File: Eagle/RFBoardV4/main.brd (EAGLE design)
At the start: 34.3 x 77.5 mm, 28 parts, among them Q1 8/16/20MHz, U1 ATMEGA328

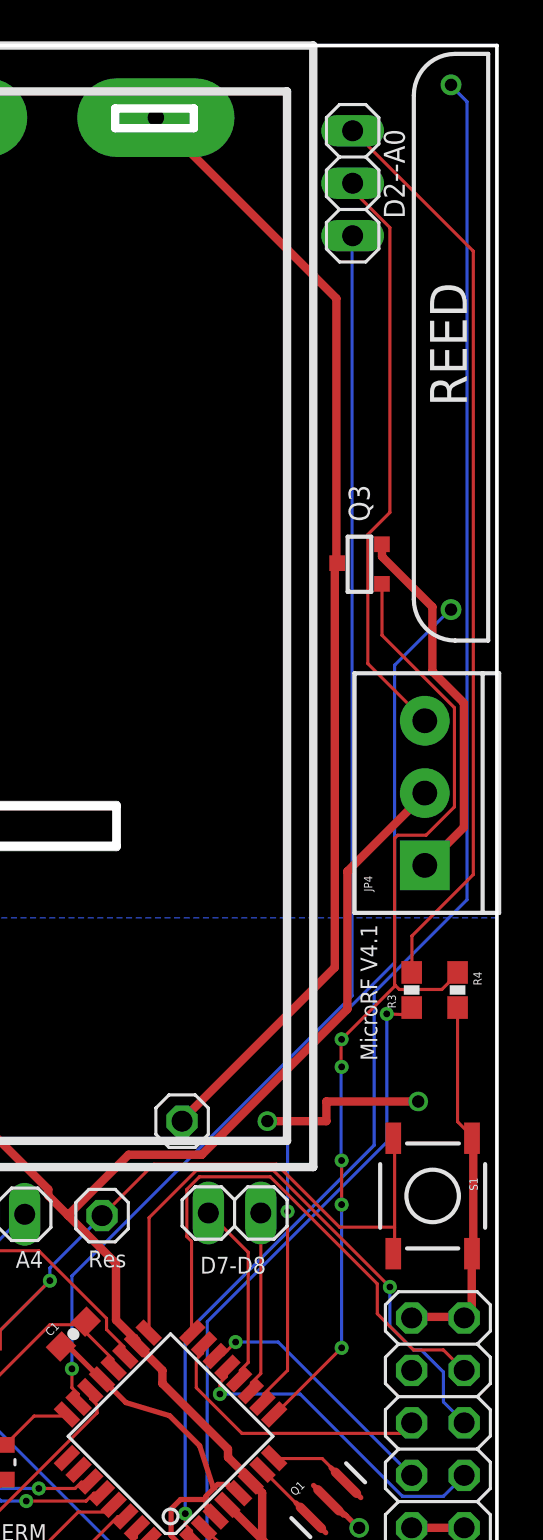
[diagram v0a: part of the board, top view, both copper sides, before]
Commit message: 4.x support + 4.1 pcb layout + cleanup
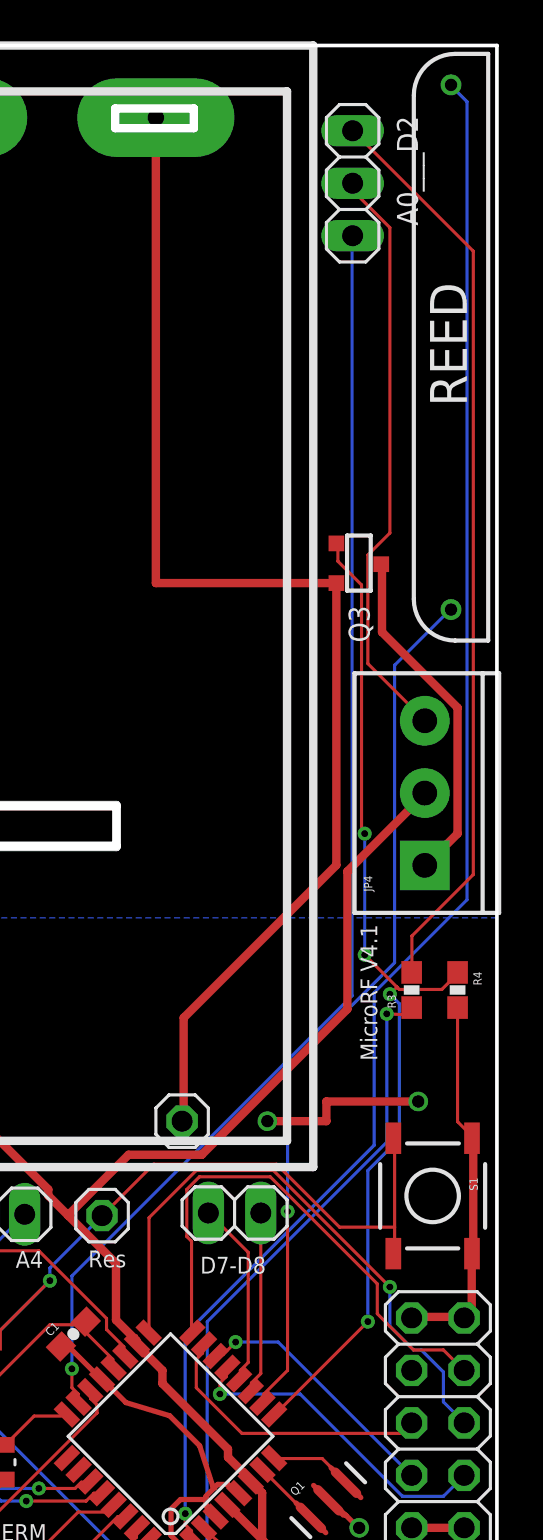
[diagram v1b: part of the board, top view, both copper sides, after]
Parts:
- turned Q3 to 270 degrees
- renumbered BATMIN to GND, BATPLUS to VCC(3V), D2--A0 to A0___D2
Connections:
- removed net SCREW_GND: JP4.1, Q3.2
- new net N$4: JP4.1, Q3.3
- net GND: now also Q3.2; no longer Q3.3
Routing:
- net SCREW_GND: track 18.0 -> 0.00 mm
- net N$4: track 0.00 -> 16.8 mm
- net GND: track 139.1 -> 144.2 mm
- net D5: track 50.2 -> 49.6 mm, vias 5 -> 4

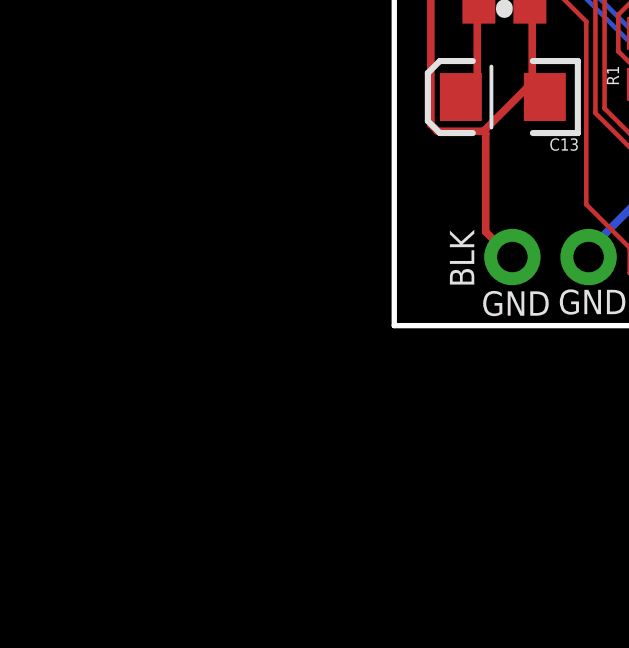
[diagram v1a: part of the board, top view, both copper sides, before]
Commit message: Adding power boost - still WIP
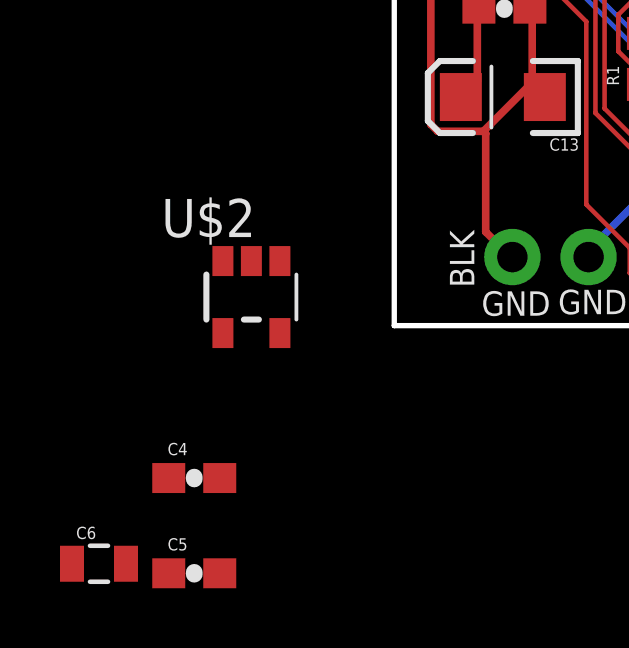
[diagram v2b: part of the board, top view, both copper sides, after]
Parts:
- added C4: 10uF, SparkFun:0603-CAP
- added C5: 4.7uF, SparkFun:0603-CAP
- added C6: 4.7uH, SparkFun:0805
- added U$2: XC9140, boost:SOT23-5
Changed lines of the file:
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@@
 <?xml version="1.0" encoding="utf-8"?>
 <!DOCTYPE eagle SYSTEM "eagle.dtd">
-<eagle version="7.2.0">
+<eagle version="7.5.0">
 <drawing>
 <settings>
@@
 <layer number="112" name="tSilk" color="7" fill="1" visible="no" active="yes"/>
 <layer number="113" name="IDFDebug" color="4" fill="1" visible="no" active="yes"/>
+<layer number="114" name="FRNTMAAT1" color="7" fill="1" visible="yes" active="yes"/>
+<layer number="115" name="FRNTMAAT2" color="7" fill="1" visible="yes" active="yes"/>
 <layer number="116" name="Patch_BOT" color="9" fill="4" visible="no" active="yes"/>
+<layer number="117" name="BACKMAAT1" color="7" fill="1" visible="yes" active="yes"/>
+<layer number="118" name="Rect_Pads" color="7" fill="1" visible="no" active="no"/>
+<layer number="119" name="KAP_TEKEN" color="7" fill="1" visible="yes" active="yes"/>
+<layer number="120" name="KAP_MAAT1" color="7" fill="1" visible="yes" active="yes"/>
 <layer number="121" name="_tsilk" color="7" fill="1" visible="no" active="yes"/>
 <layer number="122" name="_bsilk" color="7" fill="1" visible="no" active="yes"/>
@@
 <layer number="127" name="_tValues" color="7" fill="1" visible="no" active="yes"/>
 <layer number="128" name="_bValues" color="7" fill="1" visible="no" active="yes"/>
+<layer number="130" name="SMDSTROOK" color="7" fill="1" visible="yes" active="yes"/>
 <layer number="131" name="tAdjust" color="7" fill="1" visible="no" active="yes"/>
 <layer number="132" name="bAdjust" color="7" fill="1" visible="no" active="yes"/>
@@
 <layer number="223" name="223bmp" color="24" fill="1" visible="no" active="no"/>
 <layer number="224" name="224bmp" color="25" fill="1" visible="no" active="no"/>
+<layer number="225" name="225bmp" color="7" fill="1" visible="no" active="yes"/>
+<layer number="226" name="226bmp" color="7" fill="1" visible="no" active="yes"/>
+<layer number="227" name="227bmp" color="7" fill="1" visible="no" active="yes"/>
+<layer number="228" name="228bmp" color="7" fill="1" visible="no" active="yes"/>
+<layer number="230" name="230bmp" color="7" fill="1" visible="no" active="yes"/>
+<layer number="231" name="Eagle3D_PG1" color="7" fill="1" visible="yes" active="yes"/>
+<layer number="232" name="Eagle3D_PG2" color="7" fill="1" visible="yes" active="yes"/>
+<layer number="233" name="Eagle3D_PG3" color="7" fill="1" visible="yes" active="yes"/>
 <layer number="248" name="Housing" color="7" fill="1" visible="no" active="yes"/>
 <layer number="249" name="Edge" color="7" fill="1" visible="no" active="yes"/>
@@
 <layer number="251" name="SMDround" color="12" fill="11" visible="no" active="no"/>
 <layer number="254" name="cooling" color="7" fill="1" visible="no" active="yes"/>
+<layer number="255" name="Accent" color="7" fill="1" visible="yes" active="yes"/>
 </layers>
 <board>
@@
 <element name="Q3" library="transistors" package="SOT-23" value="" x="27.6225" y="52.3875" rot="R270"/>
 <element name="U$1" library="battery_wilkie" package="AAABATTERY" value="BAT" x="1.27" y="75.2475"/>
+<element name="U$2" library="boost" package="SOT23-5" value="XC9140" x="-4.7625" y="0.9525"/>
+<element name="C4" library="SparkFun" package="0603-CAP" value="10uF" x="-6.6675" y="-5.08"/>
+<element name="C5" library="SparkFun" package="0603-CAP" value="4.7uF" x="-6.6675" y="-8.255"/>
+<element name="C6" library="SparkFun" package="0805" value="4.7uH" x="-9.8425" y="-7.9375"/>
 </elements>
 <signals>

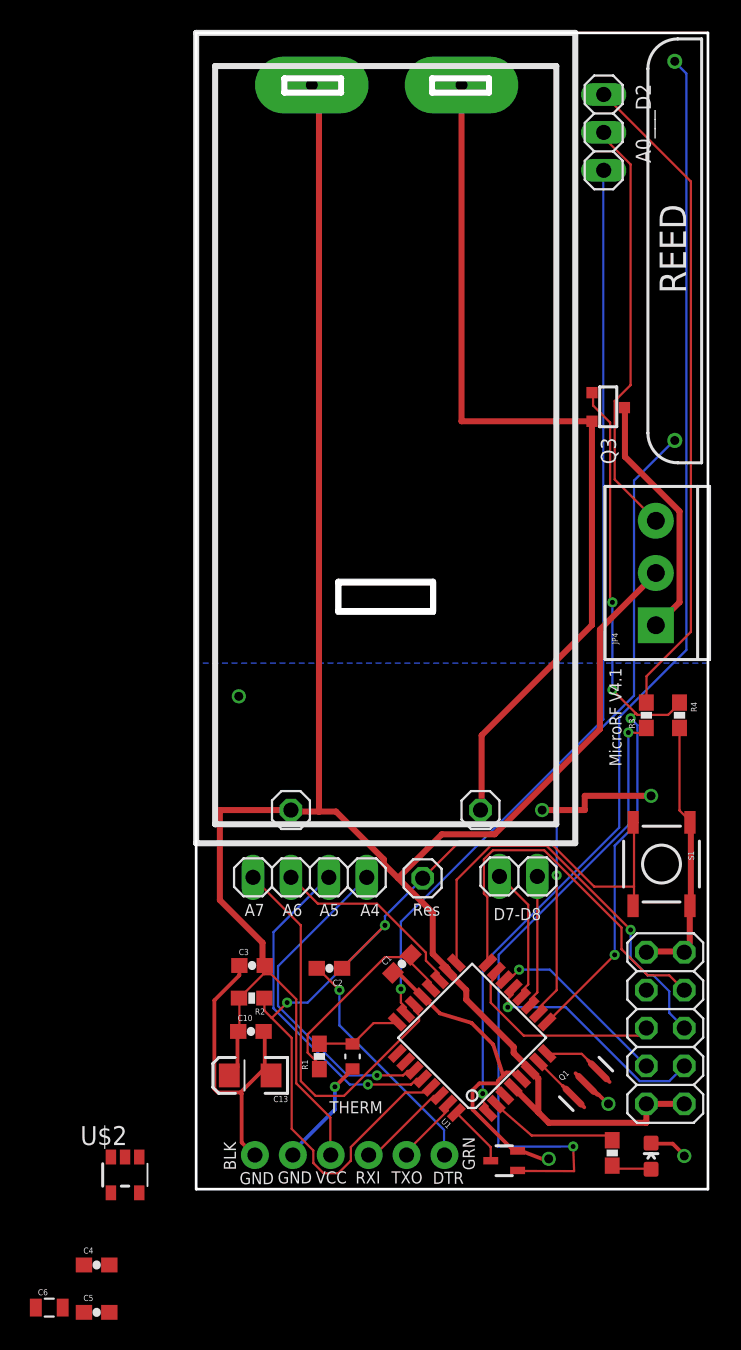
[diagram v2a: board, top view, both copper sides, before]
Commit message: Added 3.3v boost circuit to output
- removed transistor that turns aux power on/off
- used boost IC instead
- The aux power now has 3.3v and is useful for PIR solutions
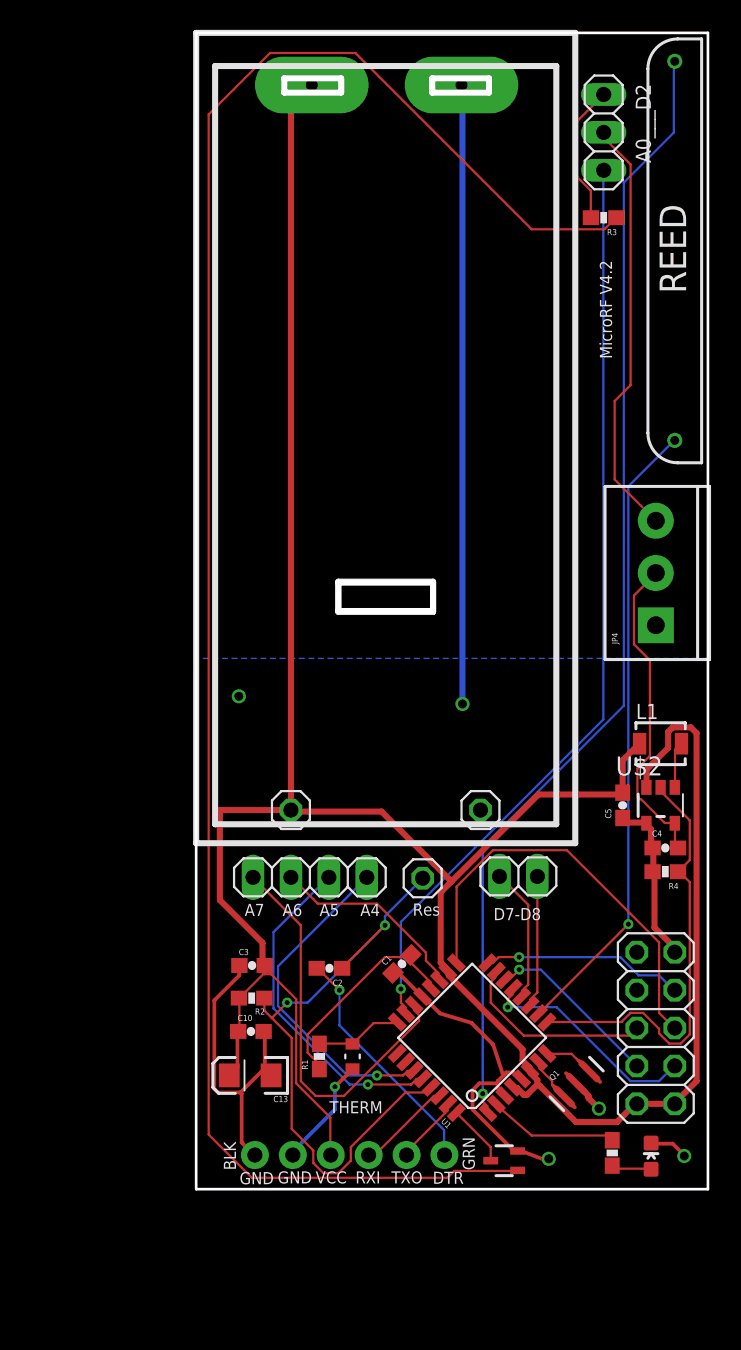
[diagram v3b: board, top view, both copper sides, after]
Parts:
- removed C6: 4.7uH, SparkFun:0805
- removed Q3: (no value), transistors:SOT-23
- removed S1: Reset, Testing:TACTILE-SWITCH-SMD-ALT01
- added L1: VLF302510MT, inductor-tdk:VLF302510MT
- moved C5 49.0 mm to (28.6, 25.7), turned to 90 degrees
- moved C4 47.2 mm to (31.4, 22.9)
- moved U$2 43.6 mm to (31.1, 25.7)
- moved R3 33.5 mm to (27.3, 65.1), turned to 180 degrees
- moved R4 10.5 mm to (31.4, 21.3), turned to 180 degrees
- moved JP5 0.64 mm to (30.8, 10.8)
- moved Q1 0.63 mm to (25.5, 7.05)
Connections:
- removed net N$4: JP4.1, Q3.3
- new net N$8: L1.2, U$2.1
- new net REG_3.3V: C4.2, JP4.2, U$2.5
- net D5: now also U$2.2; no longer Q3.1
- net GND: now also C4.1, C5.1, U$2.4; no longer Q3.2, S1.1, S1.2
- net RESET: no longer S1.3, S1.4
- net VCC: now also C5.2, L1.1, U$2.3; no longer JP4.2
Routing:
- net N$6: track 43.4 -> 124.7 mm, vias 2 -> 0
- net N$3: track 44.4 -> 9.37 mm
- net GND: track 144.2 -> 110.2 mm, vias 7 -> 6
- net RESET: track 64.0 -> 41.9 mm
- net REG_3.3V: track 0.00 -> 21.4 mm
- net D5: track 49.6 -> 29.2 mm, vias 4 -> 0
- net VCC: track 161.2 -> 181.2 mm
- net N$4: track 16.8 -> 0.00 mm
- net MISO: track 25.5 -> 13.6 mm, vias 0 -> 1
- net N$8: track 0.00 -> 3.13 mm
- net N$1: track 2.96 -> 2.31 mm
- net CE: track 15.7 -> 15.1 mm
- net REED_INT: track 76.5 -> 75.9 mm
- net MOSI: track 13.8 -> 13.2 mm
- net CSN: track 12.4 -> 11.8 mm
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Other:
- board text added: "MicroRF V4.2"
- board text removed: "MicroRF V4.1"

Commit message: V4.3 - Better option for int and reed
Added two pins for more reed options.  this also gives the ability to
choose the reverse or not for the interrupts
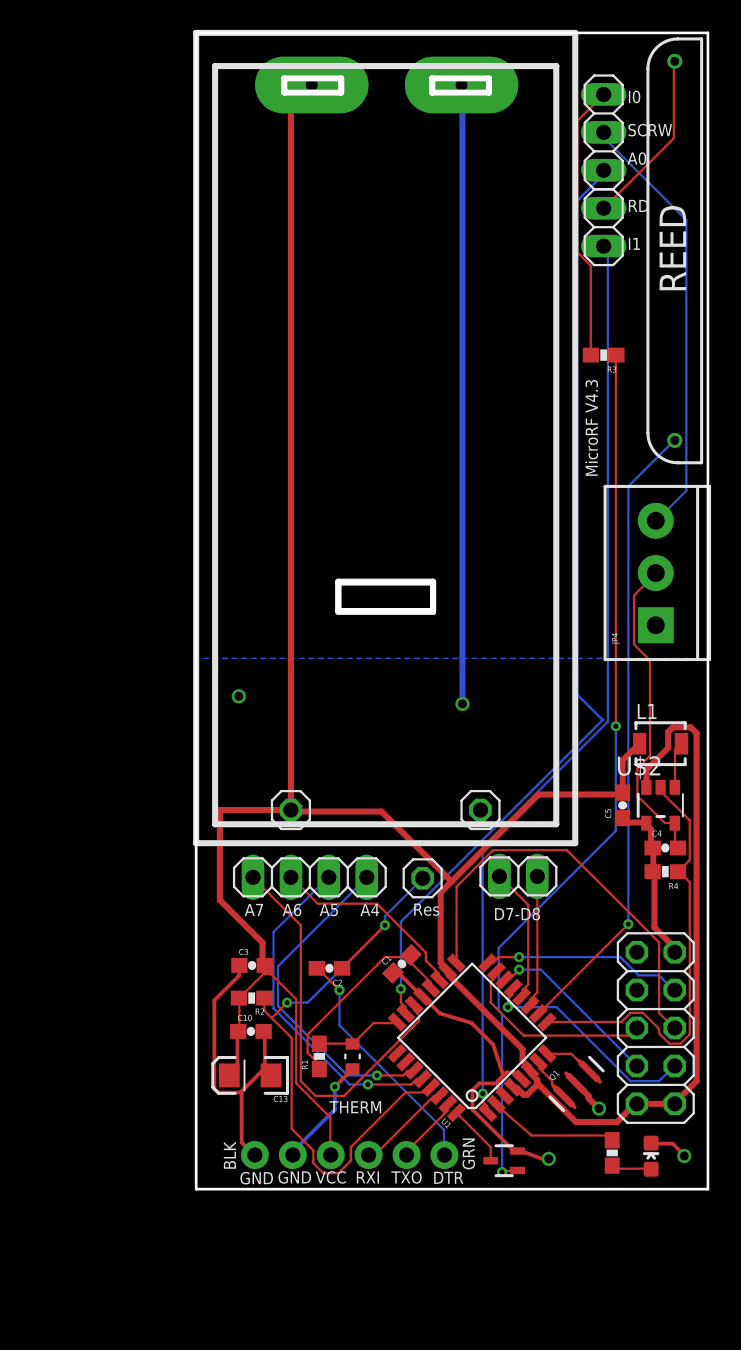
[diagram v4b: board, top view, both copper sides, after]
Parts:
- added D7-D1: (no value), pinhead:1X02
- moved R3 9.21 mm to (27.3, 55.9)
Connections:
- net N$3 renamed D2_VIA_FET
- net REED/D3 renamed REED/D6
- removed net REED_INT: S3.1, U1.1
- new net D2_INT0: U1.32
- new net D3_INT1: D7-D1.2, U1.1
- new net REED: D7-D1.1, S3.1
- net D2: no longer U1.32
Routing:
- net REED_INT: track 75.9 -> 0.00 mm, vias 1 -> 0
- net N$6: track 124.7 -> 59.2 mm, vias 0 -> 2
- net D3_INT1: track 0.00 -> 61.8 mm, vias 0 -> 1
- net REED: track 0.00 -> 11.8 mm
- net D2_VIA_FET: track 9.37 -> 18.6 mm
- net A0: track 62.5 -> 64.1 mm
- net SCREW_TERM: track 28.4 -> 29.2 mm
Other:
- board text added: "A0"
- board text added: "I0"
- board text added: "I1"
- board text added: "MicroRF V4.3"
- board text added: "RD"
- board text added: "SCRW"
- board text removed: "MicroRF V4.2"

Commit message: Fixed boost, board improvements
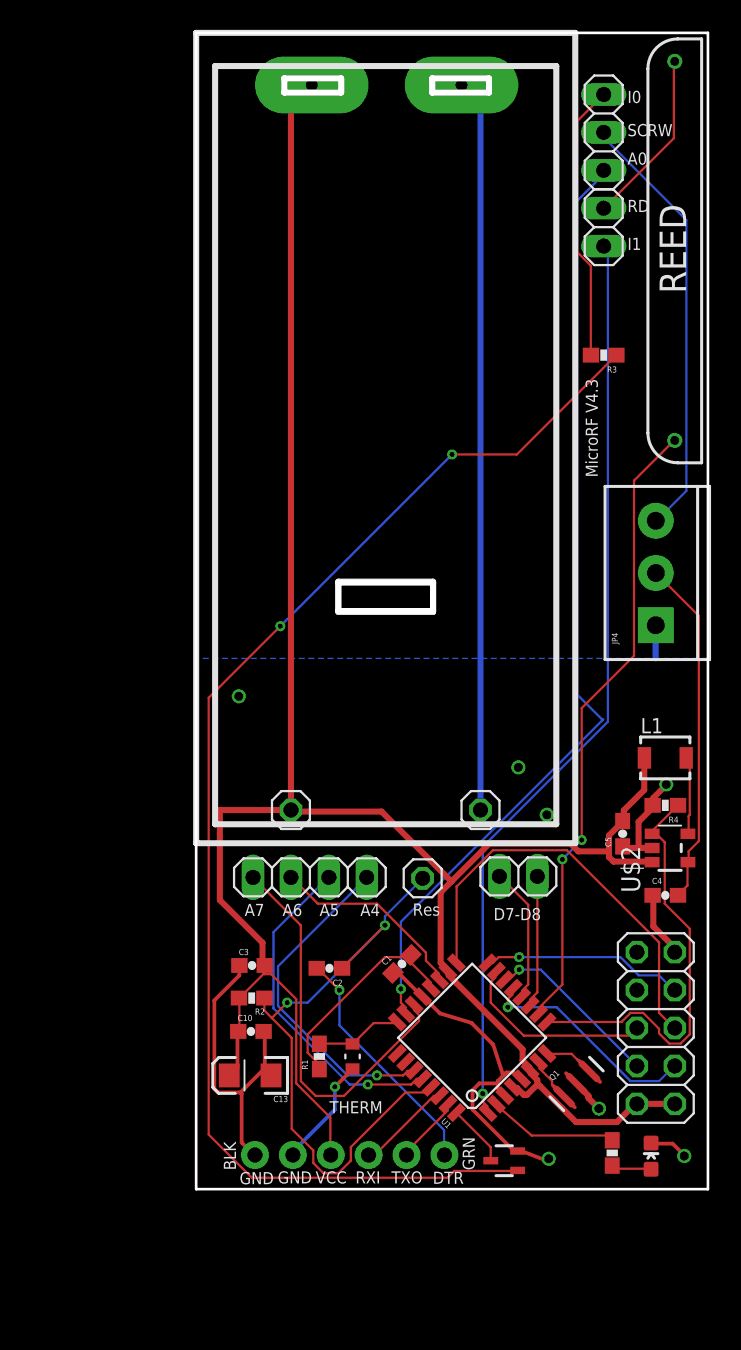
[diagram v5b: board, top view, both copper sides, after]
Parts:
- moved R4 4.45 mm to (31.4, 25.7)
- moved C4 3.18 mm to (31.4, 19.7)
- moved U$2 2.93 mm to (31.8, 22.9), turned to 90 degrees
- moved C5 1.91 mm to (28.6, 23.8)
- moved L1 1.00 mm to (31.4, 28.9)
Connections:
- net D5: now also U$2.1; no longer U$2.2
- net GND: now also JP4.1, U$2.2; no longer U$2.4
- net N$8: now also U$2.5; no longer U$2.1
- net REG_3.3V: now also U$2.4; no longer U$2.5
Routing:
- net N$6: track 59.2 -> 88.2 mm
- net VCC: track 181.2 -> 154.0 mm
- net GND: track 110.2 -> 121.0 mm, vias 6 -> 8
- net N$8: track 3.13 -> 5.23 mm
- net REG_3.3V: track 21.4 -> 23.4 mm
- net D5: track 29.2 -> 28.6 mm
- net REED/D6: vias 1 -> 2
